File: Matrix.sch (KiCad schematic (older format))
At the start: 171 parts

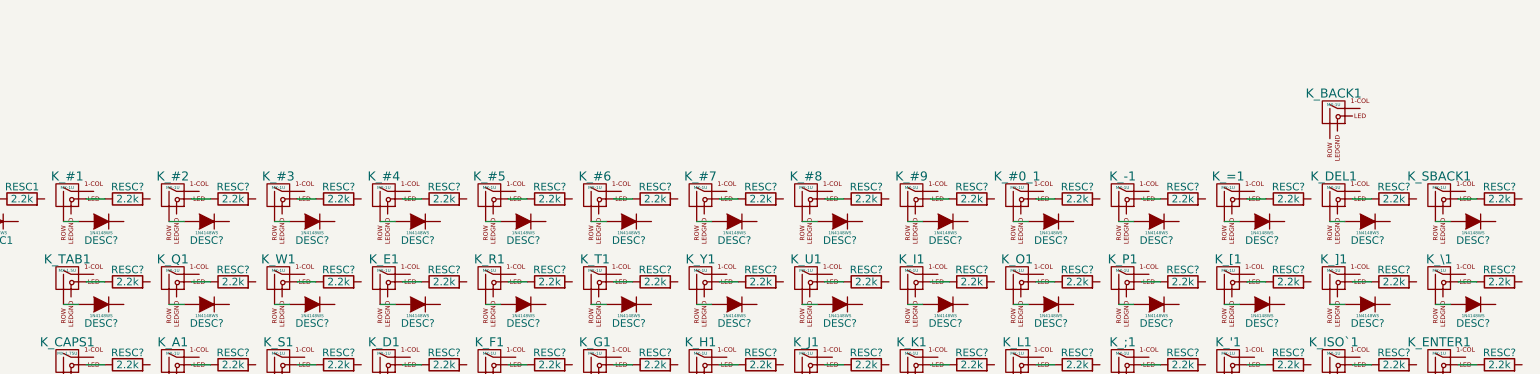
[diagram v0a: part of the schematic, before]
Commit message: Rename first row of resistors
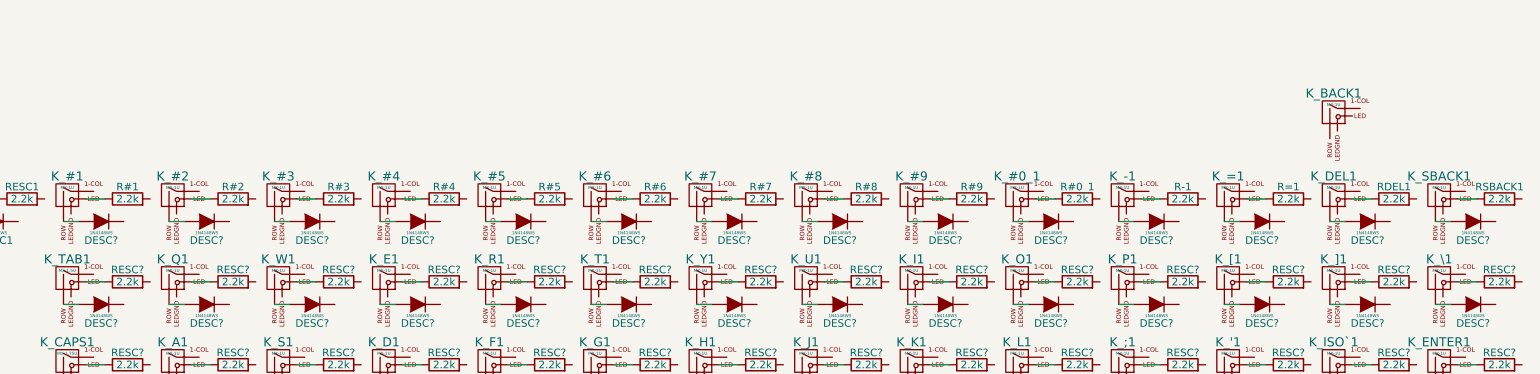
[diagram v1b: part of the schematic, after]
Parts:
- gave numbers to parts that had none: 14
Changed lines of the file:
@@
 $EndComp
 $Comp
-L R RESC?
+L R R#1
 U 1 1 5983CD6A
 P 1900 1550
-F 0 "RESC?" V 1980 1550 50  0000 C CNN
+F 0 "R#1" V 1980 1550 50  0000 C CNN
 F 1 "2.2k" V 1900 1550 50  0000 C CNN
 F 2 "" V 1830 1550 50  0001 C CNN
@@
 $EndComp
 $Comp
-L R RESC?
+L R R#2
 U 1 1 597DB09F
 P 2600 1550
-F 0 "RESC?" V 2680 1550 50  0000 C CNN
+F 0 "R#2" V 2680 1550 50  0000 C CNN
 F 1 "2.2k" V 2600 1550 50  0000 C CNN
 F 2 "" V 2530 1550 50  0001 C CNN
@@
 $EndComp
 $Comp
-L R RESC?
+L R R#3
 U 1 1 597DB0B3
 P 3300 1550
-F 0 "RESC?" V 3380 1550 50  0000 C CNN
+F 0 "R#3" V 3380 1550 50  0000 C CNN
 F 1 "2.2k" V 3300 1550 50  0000 C CNN
 F 2 "" V 3230 1550 50  0001 C CNN
@@
 $EndComp
 $Comp
-L R RESC?
+L R R#4
 U 1 1 597DB5B3
 P 4000 1550
-F 0 "RESC?" V 4080 1550 50  0000 C CNN
+F 0 "R#4" V 4080 1550 50  0000 C CNN
 F 1 "2.2k" V 4000 1550 50  0000 C CNN
 F 2 "" V 3930 1550 50  0001 C CNN
@@
 $EndComp
 $Comp
-L R RESC?
+L R R#5
 U 1 1 597DB5C7
 P 4700 1550
-F 0 "RESC?" V 4780 1550 50  0000 C CNN
+F 0 "R#5" V 4780 1550 50  0000 C CNN
 F 1 "2.2k" V 4700 1550 50  0000 C CNN
 F 2 "" V 4630 1550 50  0001 C CNN
@@
 $EndComp
 $Comp
-L R RESC?
+L R R#6
 U 1 1 597DB5DB
 P 5400 1550
-F 0 "RESC?" V 5480 1550 50  0000 C CNN
+F 0 "R#6" V 5480 1550 50  0000 C CNN
 F 1 "2.2k" V 5400 1550 50  0000 C CNN
 F 2 "" V 5330 1550 50  0001 C CNN
@@
 $EndComp
 $Comp
-L R RESC?
+L R R#7
 U 1 1 597DB5EF
 P 6100 1550
-F 0 "RESC?" V 6180 1550 50  0000 C CNN
+F 0 "R#7" V 6180 1550 50  0000 C CNN
 F 1 "2.2k" V 6100 1550 50  0000 C CNN
 F 2 "" V 6030 1550 50  0001 C CNN
@@
 $EndComp
 $Comp
-L R RESC?
+L R R#8
 U 1 1 597DF71A
 P 6800 1550
-F 0 "RESC?" V 6880 1550 50  0000 C CNN
+F 0 "R#8" V 6880 1550 50  0000 C CNN
 F 1 "2.2k" V 6800 1550 50  0000 C CNN
 F 2 "" V 6730 1550 50  0001 C CNN
@@
 $EndComp
 $Comp
-L R RESC?
+L R R#9
 U 1 1 597DF72E
 P 7500 1550
-F 0 "RESC?" V 7580 1550 50  0000 C CNN
+F 0 "R#9" V 7580 1550 50  0000 C CNN
 F 1 "2.2k" V 7500 1550 50  0000 C CNN
 F 2 "" V 7430 1550 50  0001 C CNN
@@
 $EndComp
 $Comp
-L R RESC?
+L R R#0_1
 U 1 1 597DF742
 P 8200 1550
-F 0 "RESC?" V 8280 1550 50  0000 C CNN
+F 0 "R#0_1" V 8280 1550 50  0000 C CNN
 F 1 "2.2k" V 8200 1550 50  0000 C CNN
 F 2 "" V 8130 1550 50  0001 C CNN
@@
 $EndComp
 $Comp
-L R RESC?
+L R R-1
 U 1 1 597E001A
 P 8900 1550
-F 0 "RESC?" V 8980 1550 50  0000 C CNN
+F 0 "R-1" V 8980 1550 50  0000 C CNN
 F 1 "2.2k" V 8900 1550 50  0000 C CNN
 F 2 "" V 8830 1550 50  0001 C CNN
@@
 $EndComp
 $Comp
-L R RESC?
+L R R=1
 U 1 1 597E002E
 P 9600 1550
-F 0 "RESC?" V 9680 1550 50  0000 C CNN
+F 0 "R=1" V 9680 1550 50  0000 C CNN
 F 1 "2.2k" V 9600 1550 50  0000 C CNN
 F 2 "" V 9530 1550 50  0001 C CNN
@@
 $EndComp
 $Comp
-L R RESC?
+L R RDEL1
 U 1 1 597E0042
 P 10300 1550
-F 0 "RESC?" V 10380 1550 50  0000 C CNN
+F 0 "RDEL1" V 10380 1550 50  0000 C CNN
 F 1 "2.2k" V 10300 1550 50  0000 C CNN
 F 2 "" V 10230 1550 50  0001 C CNN
@@
 $EndComp
 $Comp
-L R RESC?
+L R RSBACK1
 U 1 1 597E0056
 P 11000 1550
-F 0 "RESC?" V 11080 1550 50  0000 C CNN
+F 0 "RSBACK1" V 11080 1550 50  0000 C CNN
 F 1 "2.2k" V 11000 1550 50  0000 C CNN
 F 2 "" V 10930 1550 50  0001 C CNN

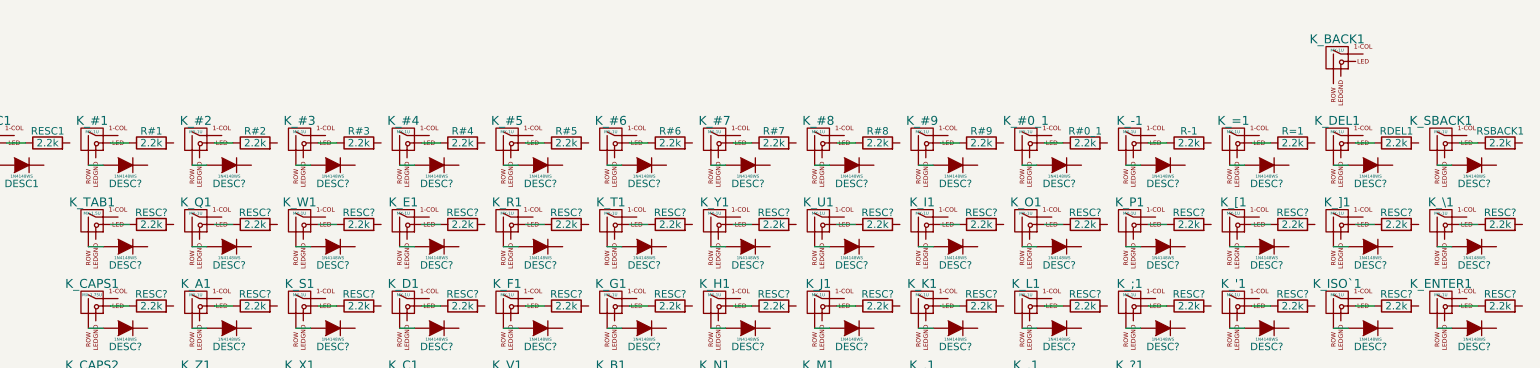
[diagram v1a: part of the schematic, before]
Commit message: Rename first row diodes
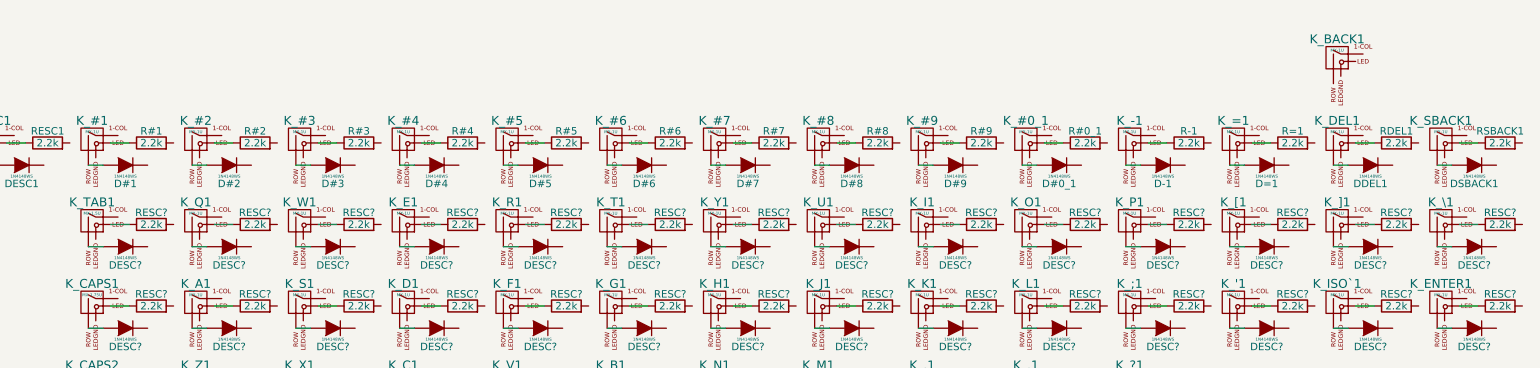
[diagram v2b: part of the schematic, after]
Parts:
- gave numbers to parts that had none: 14
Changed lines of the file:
@@
 $EndComp
 $Comp
-L D DESC?
+L D D#1
 U 1 1 5983CD70
 P 1725 1700
-F 0 "DESC?" H 1725 1825 50  0000 C CNN
+F 0 "D#1" H 1725 1825 50  0000 C CNN
 F 1 "1N4148WS" H 1725 1775 20  0000 C CNN
 F 2 "" H 1725 1700 50  0001 C CNN
@@
 $EndComp
 $Comp
-L D DESC?
+L D D#2
 U 1 1 597DB0A5
 P 2425 1700
-F 0 "DESC?" H 2425 1825 50  0000 C CNN
+F 0 "D#2" H 2425 1825 50  0000 C CNN
 F 1 "1N4148WS" H 2425 1775 20  0000 C CNN
 F 2 "" H 2425 1700 50  0001 C CNN
@@
 $EndComp
 $Comp
-L D DESC?
+L D D#3
 U 1 1 597DB0B9
 P 3125 1700
-F 0 "DESC?" H 3125 1825 50  0000 C CNN
+F 0 "D#3" H 3125 1825 50  0000 C CNN
 F 1 "1N4148WS" H 3125 1775 20  0000 C CNN
 F 2 "" H 3125 1700 50  0001 C CNN
@@
 $EndComp
 $Comp
-L D DESC?
+L D D#4
 U 1 1 597DB5B9
 P 3825 1700
-F 0 "DESC?" H 3825 1825 50  0000 C CNN
+F 0 "D#4" H 3825 1825 50  0000 C CNN
 F 1 "1N4148WS" H 3825 1775 20  0000 C CNN
 F 2 "" H 3825 1700 50  0001 C CNN
@@
 $EndComp
 $Comp
-L D DESC?
+L D D#5
 U 1 1 597DB5CD
 P 4525 1700
-F 0 "DESC?" H 4525 1825 50  0000 C CNN
+F 0 "D#5" H 4525 1825 50  0000 C CNN
 F 1 "1N4148WS" H 4525 1775 20  0000 C CNN
 F 2 "" H 4525 1700 50  0001 C CNN
@@
 $EndComp
 $Comp
-L D DESC?
+L D D#6
 U 1 1 597DB5E1
 P 5225 1700
-F 0 "DESC?" H 5225 1825 50  0000 C CNN
+F 0 "D#6" H 5225 1825 50  0000 C CNN
 F 1 "1N4148WS" H 5225 1775 20  0000 C CNN
 F 2 "" H 5225 1700 50  0001 C CNN
@@
 $EndComp
 $Comp
-L D DESC?
+L D D#7
 U 1 1 597DB5F5
 P 5925 1700
-F 0 "DESC?" H 5925 1825 50  0000 C CNN
+F 0 "D#7" H 5925 1825 50  0000 C CNN
 F 1 "1N4148WS" H 5925 1775 20  0000 C CNN
 F 2 "" H 5925 1700 50  0001 C CNN
@@
 $EndComp
 $Comp
-L D DESC?
+L D D#8
 U 1 1 597DF720
 P 6625 1700
-F 0 "DESC?" H 6625 1825 50  0000 C CNN
+F 0 "D#8" H 6625 1825 50  0000 C CNN
 F 1 "1N4148WS" H 6625 1775 20  0000 C CNN
 F 2 "" H 6625 1700 50  0001 C CNN
@@
 $EndComp
 $Comp
-L D DESC?
+L D D#9
 U 1 1 597DF734
 P 7325 1700
-F 0 "DESC?" H 7325 1825 50  0000 C CNN
+F 0 "D#9" H 7325 1825 50  0000 C CNN
 F 1 "1N4148WS" H 7325 1775 20  0000 C CNN
 F 2 "" H 7325 1700 50  0001 C CNN
@@
 $EndComp
 $Comp
-L D DESC?
+L D D#0_1
 U 1 1 597DF748
 P 8025 1700
-F 0 "DESC?" H 8025 1825 50  0000 C CNN
+F 0 "D#0_1" H 8025 1825 50  0000 C CNN
 F 1 "1N4148WS" H 8025 1775 20  0000 C CNN
 F 2 "" H 8025 1700 50  0001 C CNN
@@
 $EndComp
 $Comp
-L D DESC?
+L D D-1
 U 1 1 597E0020
 P 8725 1700
-F 0 "DESC?" H 8725 1825 50  0000 C CNN
+F 0 "D-1" H 8725 1825 50  0000 C CNN
 F 1 "1N4148WS" H 8725 1775 20  0000 C CNN
 F 2 "" H 8725 1700 50  0001 C CNN
@@
 $EndComp
 $Comp
-L D DESC?
+L D D=1
 U 1 1 597E0034
 P 9425 1700
-F 0 "DESC?" H 9425 1825 50  0000 C CNN
+F 0 "D=1" H 9425 1825 50  0000 C CNN
 F 1 "1N4148WS" H 9425 1775 20  0000 C CNN
 F 2 "" H 9425 1700 50  0001 C CNN
@@
 $EndComp
 $Comp
-L D DESC?
+L D DDEL1
 U 1 1 597E0048
 P 10125 1700
-F 0 "DESC?" H 10125 1825 50  0000 C CNN
+F 0 "DDEL1" H 10125 1825 50  0000 C CNN
 F 1 "1N4148WS" H 10125 1775 20  0000 C CNN
 F 2 "" H 10125 1700 50  0001 C CNN
@@
 $EndComp
 $Comp
-L D DESC?
+L D DSBACK1
 U 1 1 597E005C
 P 10825 1700
-F 0 "DESC?" H 10825 1825 50  0000 C CNN
+F 0 "DSBACK1" H 10825 1825 50  0000 C CNN
 F 1 "1N4148WS" H 10825 1775 20  0000 C CNN
 F 2 "" H 10825 1700 50  0001 C CNN

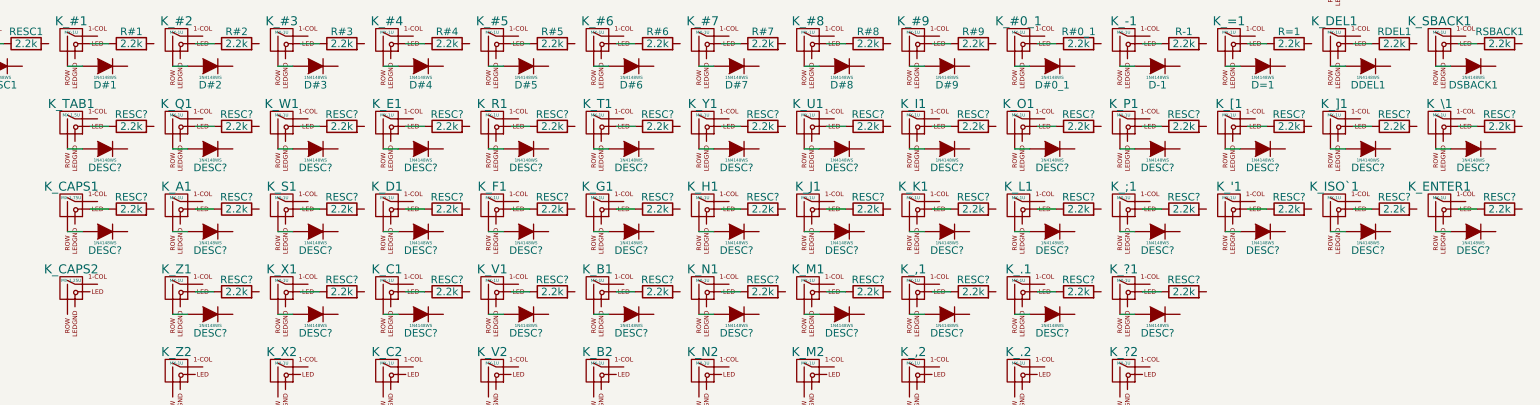
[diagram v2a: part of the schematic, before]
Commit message: Rename all resistors
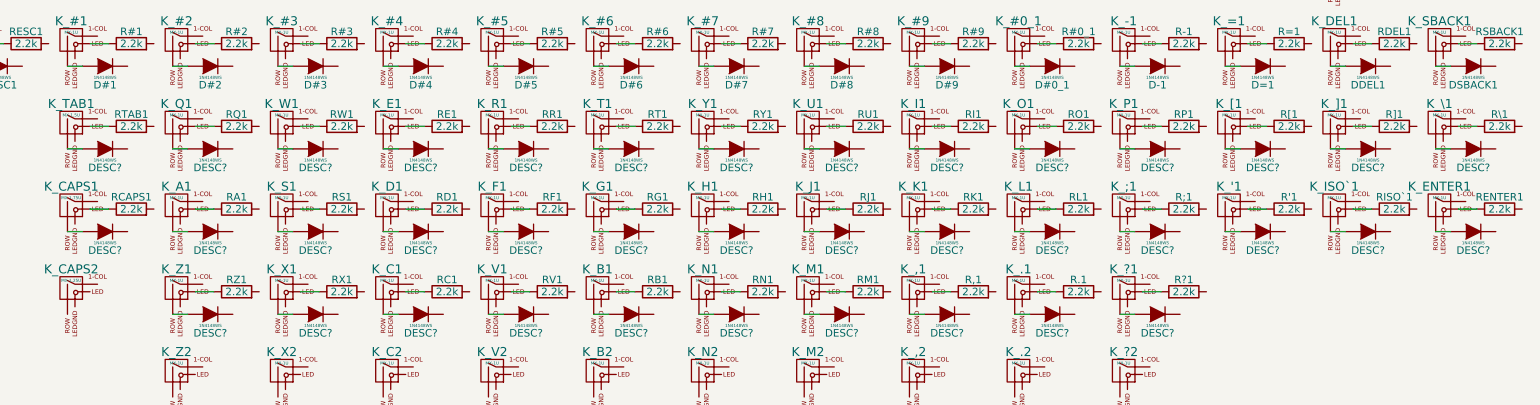
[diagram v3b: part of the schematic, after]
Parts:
- gave numbers to parts that had none: 38
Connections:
- net at K_?1.3 (LED): now also R?1.2; no longer R?1.1
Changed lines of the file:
@@
 $EndComp
 $Comp
-L R RESC?
+L R RTAB1
 U 1 1 597E3B6B
 P 1900 2100
-F 0 "RESC?" V 1980 2100 50  0000 C CNN
+F 0 "RTAB1" V 1980 2100 50  0000 C CNN
 F 1 "2.2k" V 1900 2100 50  0000 C CNN
 F 2 "" V 1830 2100 50  0001 C CNN
@@
 $EndComp
 $Comp
-L R RESC?
+L R RQ1
 U 1 1 597E3B7F
 P 2600 2100
-F 0 "RESC?" V 2680 2100 50  0000 C CNN
+F 0 "RQ1" V 2680 2100 50  0000 C CNN
 F 1 "2.2k" V 2600 2100 50  0000 C CNN
 F 2 "" V 2530 2100 50  0001 C CNN
@@
 $EndComp
 $Comp
-L R RESC?
+L R RW1
 U 1 1 597E3B93
 P 3300 2100
-F 0 "RESC?" V 3380 2100 50  0000 C CNN
+F 0 "RW1" V 3380 2100 50  0000 C CNN
 F 1 "2.2k" V 3300 2100 50  0000 C CNN
 F 2 "" V 3230 2100 50  0001 C CNN
@@
 $EndComp
 $Comp
-L R RESC?
+L R RE1
 U 1 1 597E3BA7
 P 4000 2100
-F 0 "RESC?" V 4080 2100 50  0000 C CNN
+F 0 "RE1" V 4080 2100 50  0000 C CNN
 F 1 "2.2k" V 4000 2100 50  0000 C CNN
 F 2 "" V 3930 2100 50  0001 C CNN
@@
 $EndComp
 $Comp
-L R RESC?
+L R RR1
 U 1 1 597E3BBB
 P 4700 2100
-F 0 "RESC?" V 4780 2100 50  0000 C CNN
+F 0 "RR1" V 4780 2100 50  0000 C CNN
 F 1 "2.2k" V 4700 2100 50  0000 C CNN
 F 2 "" V 4630 2100 50  0001 C CNN
@@
 $EndComp
 $Comp
-L R RESC?
+L R RT1
 U 1 1 597E3BCF
 P 5400 2100
-F 0 "RESC?" V 5480 2100 50  0000 C CNN
+F 0 "RT1" V 5480 2100 50  0000 C CNN
 F 1 "2.2k" V 5400 2100 50  0000 C CNN
 F 2 "" V 5330 2100 50  0001 C CNN
@@
 $EndComp
 $Comp
-L R RESC?
+L R RY1
 U 1 1 597E3BE3
 P 6100 2100
-F 0 "RESC?" V 6180 2100 50  0000 C CNN
+F 0 "RY1" V 6180 2100 50  0000 C CNN
 F 1 "2.2k" V 6100 2100 50  0000 C CNN
 F 2 "" V 6030 2100 50  0001 C CNN
@@
 $EndComp
 $Comp
-L R RESC?
+L R RU1
 U 1 1 597E3BF7
 P 6800 2100
-F 0 "RESC?" V 6880 2100 50  0000 C CNN
+F 0 "RU1" V 6880 2100 50  0000 C CNN
 F 1 "2.2k" V 6800 2100 50  0000 C CNN
 F 2 "" V 6730 2100 50  0001 C CNN
@@
 $EndComp
 $Comp
-L R RESC?
+L R RI1
 U 1 1 597E3C0B
 P 7500 2100
-F 0 "RESC?" V 7580 2100 50  0000 C CNN
+F 0 "RI1" V 7580 2100 50  0000 C CNN
 F 1 "2.2k" V 7500 2100 50  0000 C CNN
 F 2 "" V 7430 2100 50  0001 C CNN
@@
 $EndComp
 $Comp
-L R RESC?
+L R RO1
 U 1 1 597E3C1F
 P 8200 2100
-F 0 "RESC?" V 8280 2100 50  0000 C CNN
+F 0 "RO1" V 8280 2100 50  0000 C CNN
 F 1 "2.2k" V 8200 2100 50  0000 C CNN
 F 2 "" V 8130 2100 50  0001 C CNN
@@
 $EndComp
 $Comp
-L R RESC?
+L R RP1
 U 1 1 597E3C33
 P 8900 2100
-F 0 "RESC?" V 8980 2100 50  0000 C CNN
+F 0 "RP1" V 8980 2100 50  0000 C CNN
 F 1 "2.2k" V 8900 2100 50  0000 C CNN
 F 2 "" V 8830 2100 50  0001 C CNN
@@
 $EndComp
 $Comp
-L R RESC?
+L R R[1
 U 1 1 597E3C47
 P 9600 2100
-F 0 "RESC?" V 9680 2100 50  0000 C CNN
+F 0 "R[1" V 9680 2100 50  0000 C CNN
 F 1 "2.2k" V 9600 2100 50  0000 C CNN
 F 2 "" V 9530 2100 50  0001 C CNN
@@
 $EndComp
 $Comp
-L R RESC?
+L R R]1
 U 1 1 597E3C5B
 P 10300 2100
-F 0 "RESC?" V 10380 2100 50  0000 C CNN
+F 0 "R]1" V 10380 2100 50  0000 C CNN
 F 1 "2.2k" V 10300 2100 50  0000 C CNN
 F 2 "" V 10230 2100 50  0001 C CNN
@@
 $EndComp
 $Comp
-L R RESC?
+L R R\1
 U 1 1 597E3C6F
 P 11000 2100
-F 0 "RESC?" V 11080 2100 50  0000 C CNN
+F 0 "R\\1" V 11080 2100 50  0000 C CNN
 F 1 "2.2k" V 11000 2100 50  0000 C CNN
 F 2 "" V 10930 2100 50  0001 C CNN
@@
 $EndComp
 $Comp
-L R RESC?
+L R RCAPS1
 U 1 1 597E5CAB
 P 1900 2650
-F 0 "RESC?" V 1980 2650 50  0000 C CNN
+F 0 "RCAPS1" V 1980 2650 50  0000 C CNN
 F 1 "2.2k" V 1900 2650 50  0000 C CNN
 F 2 "" V 1830 2650 50  0001 C CNN
@@
 $EndComp
 $Comp
-L R RESC?
+L R RA1
 U 1 1 597E5CBF
 P 2600 2650
-F 0 "RESC?" V 2680 2650 50  0000 C CNN
+F 0 "RA1" V 2680 2650 50  0000 C CNN
 F 1 "2.2k" V 2600 2650 50  0000 C CNN
 F 2 "" V 2530 2650 50  0001 C CNN
@@
 $EndComp
 $Comp
-L R RESC?
+L R RS1
 U 1 1 597E5CD3
 P 3300 2650
-F 0 "RESC?" V 3380 2650 50  0000 C CNN
+F 0 "RS1" V 3380 2650 50  0000 C CNN
 F 1 "2.2k" V 3300 2650 50  0000 C CNN
 F 2 "" V 3230 2650 50  0001 C CNN
@@
 $EndComp
 $Comp
-L R RESC?
+L R RD1
 U 1 1 597E5CE7
 P 4000 2650
-F 0 "RESC?" V 4080 2650 50  0000 C CNN
+F 0 "RD1" V 4080 2650 50  0000 C CNN
 F 1 "2.2k" V 4000 2650 50  0000 C CNN
 F 2 "" V 3930 2650 50  0001 C CNN
@@
 $EndComp
 $Comp
-L R RESC?
+L R RF1
 U 1 1 597E5CFB
 P 4700 2650
-F 0 "RESC?" V 4780 2650 50  0000 C CNN
+F 0 "RF1" V 4780 2650 50  0000 C CNN
 F 1 "2.2k" V 4700 2650 50  0000 C CNN
 F 2 "" V 4630 2650 50  0001 C CNN
@@
 $EndComp
 $Comp
-L R RESC?
+L R RG1
 U 1 1 597E5D0F
 P 5400 2650
-F 0 "RESC?" V 5480 2650 50  0000 C CNN
+F 0 "RG1" V 5480 2650 50  0000 C CNN
 F 1 "2.2k" V 5400 2650 50  0000 C CNN
 F 2 "" V 5330 2650 50  0001 C CNN
@@
 $EndComp
 $Comp
-L R RESC?
+L R RH1
 U 1 1 597E5D23
 P 6100 2650
-F 0 "RESC?" V 6180 2650 50  0000 C CNN
+F 0 "RH1" V 6180 2650 50  0000 C CNN
 F 1 "2.2k" V 6100 2650 50  0000 C CNN
 F 2 "" V 6030 2650 50  0001 C CNN
@@
 $EndComp
 $Comp
-L R RESC?
+L R RJ1
 U 1 1 597E5D37
 P 6800 2650
-F 0 "RESC?" V 6880 2650 50  0000 C CNN
+F 0 "RJ1" V 6880 2650 50  0000 C CNN
 F 1 "2.2k" V 6800 2650 50  0000 C CNN
 F 2 "" V 6730 2650 50  0001 C CNN
@@
 $EndComp
 $Comp
-L R RESC?
+L R RK1
 U 1 1 597E5D4B
 P 7500 2650
-F 0 "RESC?" V 7580 2650 50  0000 C CNN
+F 0 "RK1" V 7580 2650 50  0000 C CNN
 F 1 "2.2k" V 7500 2650 50  0000 C CNN
 F 2 "" V 7430 2650 50  0001 C CNN
@@
 $EndComp
 $Comp
-L R RESC?
+L R RL1
 U 1 1 597E5D5F
 P 8200 2650
-F 0 "RESC?" V 8280 2650 50  0000 C CNN
+F 0 "RL1" V 8280 2650 50  0000 C CNN
 F 1 "2.2k" V 8200 2650 50  0000 C CNN
 F 2 "" V 8130 2650 50  0001 C CNN
@@
 $EndComp
 $Comp
-L R RESC?
+L R R;1
 U 1 1 597E5D73
 P 8900 2650
-F 0 "RESC?" V 8980 2650 50  0000 C CNN
+F 0 "R;1" V 8980 2650 50  0000 C CNN
 F 1 "2.2k" V 8900 2650 50  0000 C CNN
 F 2 "" V 8830 2650 50  0001 C CNN
@@
 $EndComp
 $Comp
-L R RESC?
+L R R'1
 U 1 1 597E5D87
 P 9600 2650
-F 0 "RESC?" V 9680 2650 50  0000 C CNN
+F 0 "R'1" V 9680 2650 50  0000 C CNN
 F 1 "2.2k" V 9600 2650 50  0000 C CNN
 F 2 "" V 9530 2650 50  0001 C CNN
@@
 $EndComp
 $Comp
-L R RESC?
+L R RISO`1
 U 1 1 597E5D9B
 P 10300 2650
-F 0 "RESC?" V 10380 2650 50  0000 C CNN
+F 0 "RISO`1" V 10380 2650 50  0000 C CNN
 F 1 "2.2k" V 10300 2650 50  0000 C CNN
 F 2 "" V 10230 2650 50  0001 C CNN
@@
 $EndComp
 $Comp
-L R RESC?
+L R RENTER1
 U 1 1 597E5DAF
 P 11000 2650
-F 0 "RESC?" V 11080 2650 50  0000 C CNN
+F 0 "RENTER1" V 11080 2650 50  0000 C CNN
 F 1 "2.2k" V 11000 2650 50  0000 C CNN
 F 2 "" V 10930 2650 50  0001 C CNN
@@
 $EndComp
 $Comp
-L R RESC?
+L R RZ1
 U 1 1 597E5DD7
 P 2600 3200
-F 0 "RESC?" V 2680 3200 50  0000 C CNN
+F 0 "RZ1" V 2680 3200 50  0000 C CNN
 F 1 "2.2k" V 2600 3200 50  0000 C CNN
 F 2 "" V 2530 3200 50  0001 C CNN
@@
 $EndComp
 $Comp
-L R RESC?
+L R RX1
 U 1 1 597E5DEB
 P 3300 3200
-F 0 "RESC?" V 3380 3200 50  0000 C CNN
+F 0 "RX1" V 3380 3200 50  0000 C CNN
 F 1 "2.2k" V 3300 3200 50  0000 C CNN
 F 2 "" V 3230 3200 50  0001 C CNN
@@
 $EndComp
 $Comp
-L R RESC?
+L R RC1
 U 1 1 597E5DFF
 P 4000 3200
-F 0 "RESC?" V 4080 3200 50  0000 C CNN
+F 0 "RC1" V 4080 3200 50  0000 C CNN
 F 1 "2.2k" V 4000 3200 50  0000 C CNN
 F 2 "" V 3930 3200 50  0001 C CNN
@@
 $EndComp
 $Comp
-L R RESC?
+L R RV1
 U 1 1 597E5E13
 P 4700 3200
-F 0 "RESC?" V 4780 3200 50  0000 C CNN
+F 0 "RV1" V 4780 3200 50  0000 C CNN
 F 1 "2.2k" V 4700 3200 50  0000 C CNN
 F 2 "" V 4630 3200 50  0001 C CNN
@@
 $EndComp
 $Comp
-L R RESC?
+L R RB1
 U 1 1 597E5E27
 P 5400 3200
-F 0 "RESC?" V 5480 3200 50  0000 C CNN
+F 0 "RB1" V 5480 3200 50  0000 C CNN
 F 1 "2.2k" V 5400 3200 50  0000 C CNN
 F 2 "" V 5330 3200 50  0001 C CNN
@@
 $EndComp
 $Comp
-L R RESC?
+L R RN1
 U 1 1 597E5E3B
 P 6100 3200
-F 0 "RESC?" V 6180 3200 50  0000 C CNN
+F 0 "RN1" V 6180 3200 50  0000 C CNN
 F 1 "2.2k" V 6100 3200 50  0000 C CNN
 F 2 "" V 6030 3200 50  0001 C CNN
@@
 $EndComp
 $Comp
-L R RESC?
+L R RM1
 U 1 1 597E5E4F
 P 6800 3200
-F 0 "RESC?" V 6880 3200 50  0000 C CNN
+F 0 "RM1" V 6880 3200 50  0000 C CNN
 F 1 "2.2k" V 6800 3200 50  0000 C CNN
 F 2 "" V 6730 3200 50  0001 C CNN
@@
 $EndComp
 $Comp
-L R RESC?
+L R R,1
 U 1 1 597E5E63
 P 7500 3200
-F 0 "RESC?" V 7580 3200 50  0000 C CNN
+F 0 "R,1" V 7580 3200 50  0000 C CNN
 F 1 "2.2k" V 7500 3200 50  0000 C CNN
 F 2 "" V 7430 3200 50  0001 C CNN
@@
 $EndComp
 $Comp
-L R RESC?
+L R R.1
 U 1 1 597E5E77
 P 8200 3200
-F 0 "RESC?" V 8280 3200 50  0000 C CNN
+F 0 "R.1" V 8280 3200 50  0000 C CNN
 F 1 "2.2k" V 8200 3200 50  0000 C CNN
 F 2 "" V 8130 3200 50  0001 C CNN
@@
 $EndComp
 $Comp
-L R RESC?
+L R R?1
 U 1 1 597E5E8B
 P 8900 3200
-F 0 "RESC?" V 8980 3200 50  0000 C CNN
+F 0 "R?1" V 8980 3200 50  0000 C CNN
 F 1 "2.2k" V 8900 3200 50  0000 C CNN
 F 2 "" V 8830 3200 50  0001 C CNN
 F 3 "" H 8900 3200 50  0001 C CNN
 	1    8900 3200
-	0    -1   -1   0
-$EndComp
-$Comp
+	0    1    -1   0
+$EndComp
+$Comp
